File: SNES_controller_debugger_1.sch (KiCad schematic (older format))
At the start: 22 parts, among them J1 ICSP, J2 CONTROLLER_OUT, J3 MICRO_USB, SW1 Reset_switch, U1 ATmega32U4, Y1 16MHz

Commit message: pcb: Another complete overhaul under the supervision of Icchan^.
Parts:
- removed R4: 4.7k, Resistors_SMD:R_0603_HandSoldering, symbol R_Small
- R1: value 200k -> 10k
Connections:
- net RESET: now also SW1.2
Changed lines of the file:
@@
 P 650 3000
 F 0 "R1" H 680 3020 50  0000 L CNN
-F 1 "200k" H 680 2960 50  0000 L CNN
+F 1 "10k" H 680 2960 50  0000 L CNN
 F 2 "Resistors_SMD:R_0603_HandSoldering" H 650 3000 50  0001 C CNN
 F 3 "" H 650 3000 50  0001 C CNN
@@
 Text GLabel 4900 5750 2    50   Output ~ 0
 VCC
-Wire Wire Line
-	6450 4650 6450 4700
-Wire Wire Line
-	6450 4700 6500 4700
-Connection ~ 7600 4850
-Wire Wire Line
-	7600 4750 7600 4850
-Connection ~ 4350 5750
-Wire Wire Line
-	4350 5750 4900 5750
-Wire Wire Line
-	4350 5550 4250 5550
-Wire Wire Line
-	4350 5550 4350 5900
-Wire Wire Line
-	4350 5900 4250 5900
-Wire Wire Line
-	6950 3200 6950 3250
-Connection ~ 7200 5450
-Wire Wire Line
-	7850 4850 8050 4850
-Wire Wire Line
-	7500 4850 7650 4850
-Wire Wire Line
-	1350 3300 1250 3300
-Wire Wire Line
-	650  3100 650  3400
-Connection ~ 850  3400
-Wire Wire Line
-	7100 5450 7400 5450
-Wire Wire Line
-	1250 1800 1500 1800
-Wire Wire Line
-	1250 1700 1500 1700
-Connection ~ 1250 1800
-Wire Wire Line
-	1250 1900 1500 1900
-Connection ~ 1250 1900
-Wire Wire Line
-	1250 1600 1500 1600
-Connection ~ 1250 1700
-Wire Wire Line
-	7200 3050 7200 2550
-Wire Wire Line
-	7350 3200 7400 3200
-Wire Wire Line
-	7400 3200 7400 3250
-Wire Wire Line
-	7050 3200 6950 3200
-Wire Wire Line
-	1250 1600 1250 2050
-Wire Wire Line
-	1050 2400 1500 2400
-Wire Wire Line
-	1050 2700 1500 2700
-Wire Wire Line
-	6000 5950 5900 5950
-Connection ~ 1250 2400
-Connection ~ 1250 2700
-Wire Wire Line
-	850  2400 750  2400
-Wire Wire Line
-	750  2400 750  2700
-Wire Wire Line
-	750  2700 850  2700
-Wire Wire Line
-	750  2550 650  2550
-Connection ~ 750  2550
-Wire Wire Line
-	650  3100 1500 3100
-Wire Wire Line
-	1500 4200 1300 4200
-Wire Wire Line
-	1300 4200 1300 4500
-Connection ~ 1300 4500
-Wire Wire Line
-	1300 4400 1500 4400
-Connection ~ 1300 4400
-Wire Wire Line
-	1500 4300 1300 4300
-Connection ~ 1300 4300
-Wire Wire Line
-	1500 4100 850  4100
-Wire Wire Line
-	1500 3800 1450 3800
-Wire Wire Line
-	1450 3800 1450 3900
-Wire Wire Line
-	1400 3900 1500 3900
-Connection ~ 1450 3900
-Wire Wire Line
-	7500 5050 7650 5050
-Wire Wire Line
-	7500 5150 7600 5150
-Wire Wire Line
-	7600 5150 7600 5300
-Wire Wire Line
-	7600 5300 7650 5300
-Wire Wire Line
-	7850 5050 8050 5050
-Wire Wire Line
-	7850 5300 8050 5300
-Wire Wire Line
-	1500 3400 850  3400
-Wire Wire Line
-	850  3300 850  3700
-Wire Wire Line
-	1500 3500 1200 3500
-Wire Wire Line
-	850  3500 1000 3500
-Connection ~ 850  3500
 Text GLabel 650  2900 1    50   Input ~ 0
 VCC
@@
 	1    0    0    -1
 $EndComp
-Wire Wire Line
-	4550 5700 4550 5750
-Connection ~ 4550 5750
 $Comp
 L Earth #PWR015
@@
 	1    0    0    -1
 $EndComp
-Wire Wire Line
-	3950 2400 4450 2400
 $Comp
 L C_Small C7
@@
 	1    0    0    -1
 $EndComp
-Wire Wire Line
-	4750 5800 4750 5750
-Connection ~ 4750 5750
 $Comp
 L Earth #PWR016
@@
 	1    0    0    -1
 $EndComp
-Wire Wire Line
-	750  4500 1500 4500
-Wire Wire Line
-	1200 4500 1200 4550
-Wire Wire Line
-	950  4500 950  4550
-Connection ~ 1200 4500
-Connection ~ 950  4500
 $Comp
 L Earth #PWR017
@@
 $EndComp
 Wire Wire Line
+	6450 4650 6450 4700
+Wire Wire Line
+	6450 4700 6500 4700
+Connection ~ 7600 4850
+Wire Wire Line
+	7600 4750 7600 4850
+Connection ~ 4350 5750
+Wire Wire Line
+	4350 5750 4900 5750
+Wire Wire Line
+	4350 5550 4250 5550
+Wire Wire Line
+	4350 5550 4350 5900
+Wire Wire Line
+	4350 5900 4250 5900
+Wire Wire Line
+	6950 3200 6950 3250
+Connection ~ 7200 5450
+Wire Wire Line
+	7850 4850 8050 4850
+Wire Wire Line
+	7500 4850 7650 4850
+Wire Wire Line
+	1350 3300 1250 3300
+Wire Wire Line
+	650  3100 650  3400
+Connection ~ 850  3400
+Wire Wire Line
+	7100 5450 7400 5450
+Wire Wire Line
+	1250 1800 1500 1800
+Wire Wire Line
+	1250 1700 1500 1700
+Connection ~ 1250 1800
+Wire Wire Line
+	1250 1900 1500 1900
+Connection ~ 1250 1900
+Wire Wire Line
+	1250 1600 1500 1600
+Connection ~ 1250 1700
+Wire Wire Line
+	7200 3050 7200 2550
+Wire Wire Line
+	7350 3200 7400 3200
+Wire Wire Line
+	7400 3200 7400 3250
+Wire Wire Line
+	7050 3200 6950 3200
+Wire Wire Line
+	1250 1600 1250 2050
+Wire Wire Line
+	1050 2400 1500 2400
+Wire Wire Line
+	1050 2700 1500 2700
+Wire Wire Line
+	6000 5950 5900 5950
+Connection ~ 1250 2400
+Connection ~ 1250 2700
+Wire Wire Line
+	850  2400 750  2400
+Wire Wire Line
+	750  2400 750  2700
+Wire Wire Line
+	750  2700 850  2700
+Wire Wire Line
+	750  2550 650  2550
+Connection ~ 750  2550
+Wire Wire Line
+	650  3100 1500 3100
+Wire Wire Line
+	1500 4200 1300 4200
+Wire Wire Line
+	1300 4200 1300 4500
+Connection ~ 1300 4500
+Wire Wire Line
+	1300 4400 1500 4400
+Connection ~ 1300 4400
+Wire Wire Line
+	1500 4300 1300 4300
+Connection ~ 1300 4300
+Wire Wire Line
+	1500 4100 850  4100
+Wire Wire Line
+	1500 3800 1450 3800
+Wire Wire Line
+	1450 3800 1450 3900
+Wire Wire Line
+	1400 3900 1500 3900
+Connection ~ 1450 3900
+Wire Wire Line
+	7500 5050 7650 5050
+Wire Wire Line
+	7500 5150 7600 5150
+Wire Wire Line
+	7600 5150 7600 5300
+Wire Wire Line
+	7600 5300 7650 5300
+Wire Wire Line
+	7850 5050 8050 5050
+Wire Wire Line
+	7850 5300 8050 5300
+Wire Wire Line
+	1500 3400 850  3400
+Wire Wire Line
+	850  3300 850  3700
+Wire Wire Line
+	1500 3500 1200 3500
+Wire Wire Line
+	850  3500 1000 3500
+Connection ~ 850  3500
+Wire Wire Line
+	4550 5700 4550 5750
+Connection ~ 4550 5750
+Wire Wire Line
+	3950 2400 4450 2400
+Wire Wire Line
+	4750 5800 4750 5750
+Connection ~ 4750 5750
+Wire Wire Line
+	750  4500 1500 4500
+Wire Wire Line
+	1200 4500 1200 4550
+Wire Wire Line
+	950  4500 950  4550
+Connection ~ 1200 4500
+Connection ~ 950  4500
+Wire Wire Line
 	1200 4800 1200 4750
 Wire Wire Line
@@
 Wire Wire Line
 	1200 4800 950  4800
-$Comp
-L R_Small R4
-U 1 1 59306BE3
-P 1350 3200
-F 0 "R4" H 1380 3220 50  0000 L CNN
-F 1 "4.7k" H 1380 3160 50  0000 L CNN
-F 2 "Resistors_SMD:R_0603_HandSoldering" H 1350 3200 50  0001 C CNN
-F 3 "" H 1350 3200 50  0001 C CNN
-	1    1350 3200
-	1    0    0    -1
-$EndComp
 Connection ~ 1350 3100
 Connection ~ 650  3100
+Wire Wire Line
+	1350 3100 1350 3300
 $EndSCHEMATC

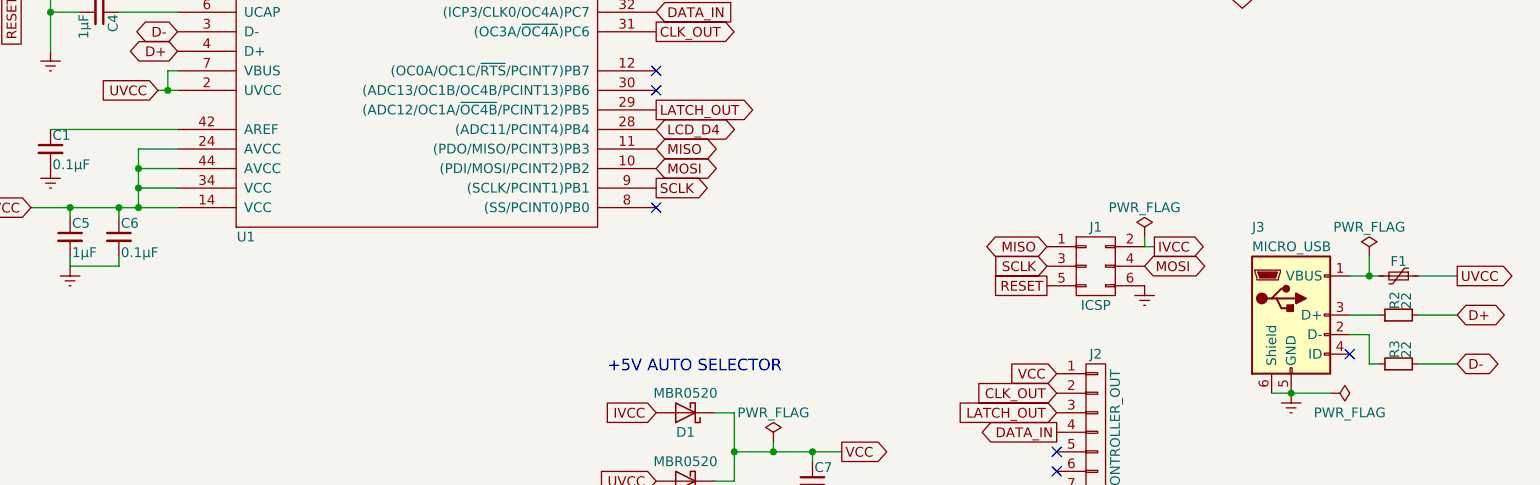
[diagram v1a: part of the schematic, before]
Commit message: pcb: Add Digi-Key part numbers and MPNs to some components
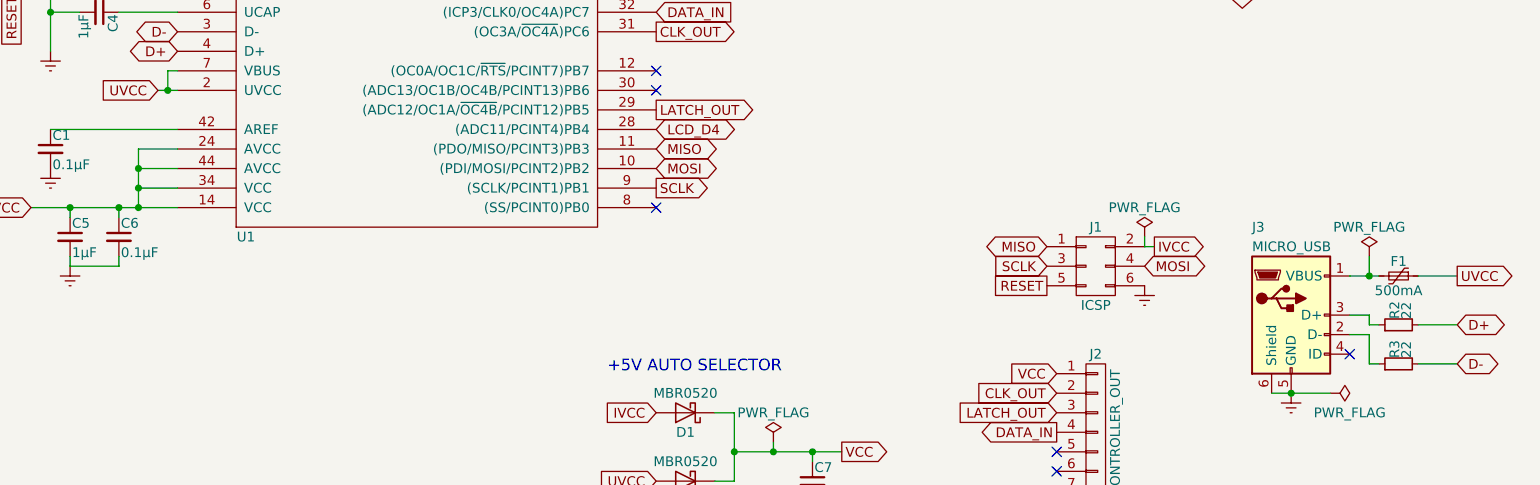
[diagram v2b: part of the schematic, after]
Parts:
- F1: value Polyfuse -> 500mA
- J3: Digi-Key part number (none) -> 609-4618-1-ND; MPN (none) -> 10118194-0001LF
- RV1: Digi-Key part number (none) -> TS53YL-10KCT-ND; MPN (none) -> TS53YL103MR10
- SW1: Digi-Key part number (none) -> 679-2428-ND; MPN (none) -> MJTP1230
- U1: Digi-Key part number (none) -> ATMEGA32U4-AU-ND; MPN (none) -> ATMEGA32U4-AU
- Y1: Digi-Key part number (none) -> 644-1187-1-ND; MPN (none) -> NX5032GA-16MHZ-STD-CSK-4
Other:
- moved on the sheet: R2
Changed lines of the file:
@@
 F 2 "Housings_QFP:TQFP-44_10x10mm_Pitch0.8mm" V 2500 2550 50  0000 C CNN
 F 3 "" H 3950 4050 50  0000 C CNN
+F 4 "ATMEGA32U4-AU-ND" H 2750 2950 60  0001 C CNN "Digi-Key part number"
+F 5 "ATMEGA32U4-AU" H 2750 2950 60  0001 C CNN "MPN"
 	1    2750 2950
 	1    0    0    1
@@
 F 2 "Megaris_fixed_footprints:Potentiometer_Trimmer_Vishay_TS53YL" H 7200 3200 50  0001 C CNN
 F 3 "" H 7200 3200 50  0001 C CNN
+F 4 "TS53YL-10KCT-ND" V 7200 3200 60  0001 C CNN "Digi-Key part number"
+F 5 "TS53YL103MR10" V 7200 3200 60  0001 C CNN "MPN"
 	1    7200 3200
 	0    1    -1   0
@@
 F 2 "Crystals:Crystal_SMD_5032-2pin_5.0x3.2mm_HandSoldering" H 1250 2550 50  0001 C CNN
 F 3 "" H 1250 2550 50  0001 C CNN
+F 4 "644-1187-1-ND" H 1250 2550 60  0001 C CNN "Digi-Key part number"
+F 5 "NX5032GA-16MHZ-STD-CSK-4" H 1250 2550 60  0001 C CNN "MPN"
 	1    1250 2550
 	0    1    1    0
@@
 L R_Small R2
 U 1 1 591C87EF
-P 7750 5050
-F 0 "R2" H 7780 5070 50  0000 L CNN
-F 1 "22" H 7780 5010 50  0000 L CNN
-F 2 "Resistors_SMD:R_0805_HandSoldering" H 7750 5050 50  0001 C CNN
-F 3 "" H 7750 5050 50  0001 C CNN
-	1    7750 5050
+P 7750 5100
+F 0 "R2" H 7780 5120 50  0000 L CNN
+F 1 "22" H 7780 5060 50  0000 L CNN
+F 2 "Resistors_SMD:R_0805_HandSoldering" H 7750 5100 50  0001 C CNN
+F 3 "" H 7750 5100 50  0001 C CNN
+	1    7750 5100
 	0    -1   -1   0
 $EndComp
@@
 Text GLabel 8050 5300 2    50   BiDi ~ 0
 D-
-Text GLabel 8050 5050 2    50   BiDi ~ 0
+Text GLabel 8050 5100 2    50   BiDi ~ 0
 D+
 $Comp
@@
 F 2 "Megaris_fixed_footprints:Conn_USBmicro-B_Amphenol_10118194-0001LF" H 7350 5000 50  0001 C CNN
 F 3 "" H 7350 5000 50  0001 C CNN
+F 4 "609-4618-1-ND" H 7200 5050 60  0001 C CNN "Digi-Key part number"
+F 5 "10118194-0001LF" H 7200 5050 60  0001 C CNN "MPN"
 	1    7200 5050
 	1    0    0    -1
@@
 P 7750 4850
 F 0 "F1" V 7675 4850 50  0000 C CNN
-F 1 "Polyfuse" V 7825 4850 50  0001 C CNN
+F 1 "500mA" V 7825 4850 50  0000 C CNN
 F 2 "Resistors_SMD:R_0603_HandSoldering" H 7800 4650 50  0001 L CNN
 F 3 "" H 7750 4850 50  0001 C CNN
@@
 F 2 "Buttons_Switches_THT:SW_PUSH_6mm" H 1050 3500 50  0001 C CNN
 F 3 "" H 1050 3500 50  0001 C CNN
+F 4 "679-2428-ND" H 1050 3300 60  0001 C CNN "Digi-Key part number"
+F 5 "MJTP1230" H 1050 3300 60  0001 C CNN "MPN"
 	1    1050 3300
 	1    0    0    -1
@@
 	1500 4200 1300 4200
 Wire Wire Line
-	1300 4200 1300 4500
+	1300 4500 1300 4200
 Connection ~ 1300 4500
 Wire Wire Line
@@
 Connection ~ 1450 3900
 Wire Wire Line
-	7500 5050 7650 5050
-Wire Wire Line
 	7500 5150 7600 5150
 Wire Wire Line
@@
 	7600 5300 7650 5300
 Wire Wire Line
-	7850 5050 8050 5050
+	7850 5100 8050 5100
 Wire Wire Line
 	7850 5300 8050 5300
@@
 Wire Wire Line
 	1350 3100 1350 3300
+Wire Wire Line
+	7500 5050 7600 5050
+Wire Wire Line
+	7600 5050 7600 5100
+Wire Wire Line
+	7600 5100 7650 5100
 $EndSCHEMATC
